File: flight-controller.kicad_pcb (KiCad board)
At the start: 2 copper layers, 51 x 54 mm, 32 parts, among them J1 XT60PW-M, J2 SM04B-SRSS-TB, J3 XT60PW-F, J4 XT60PW-F, J5 XT60PW-F, J6 XT60PW-F, U1 ACS773LCB-100B-PFF, U2 LMR33630ADDA, U3 AMS1117-3.3

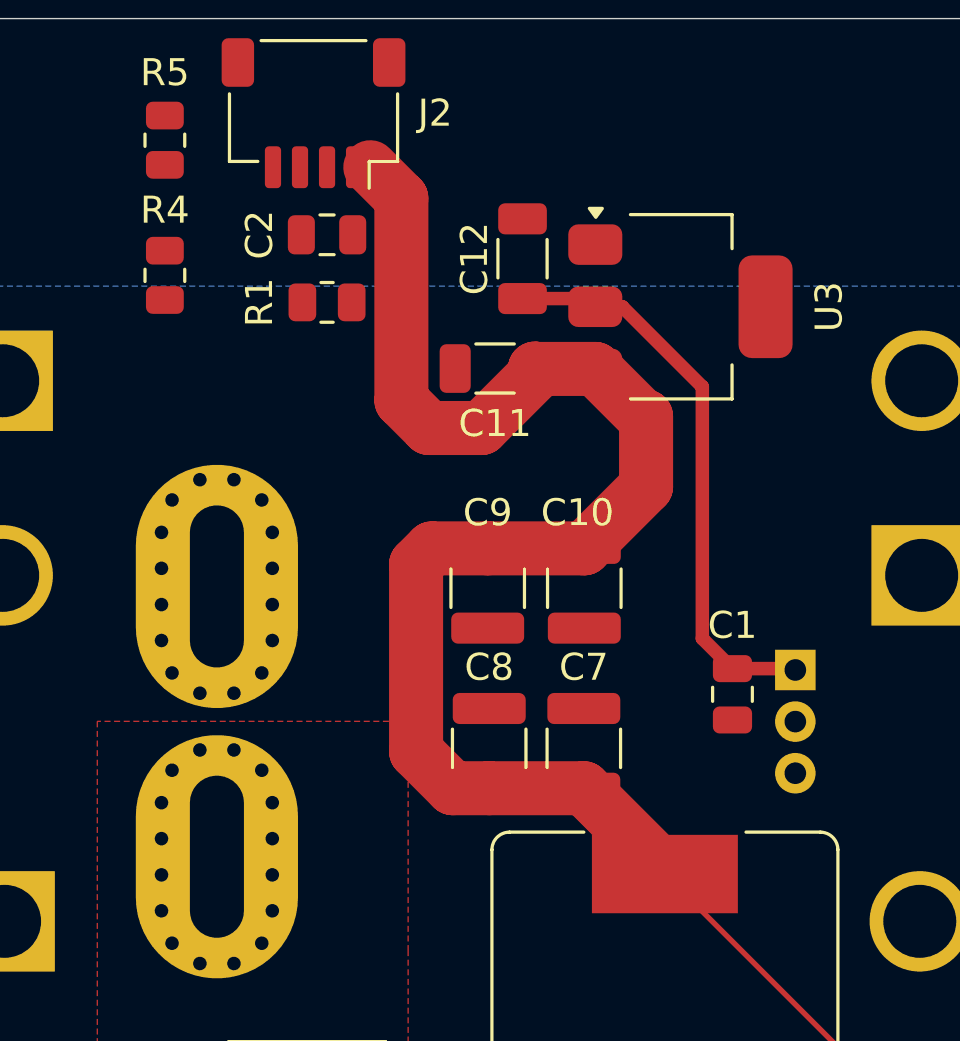
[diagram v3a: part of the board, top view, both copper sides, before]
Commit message: feat: Routed analog signals
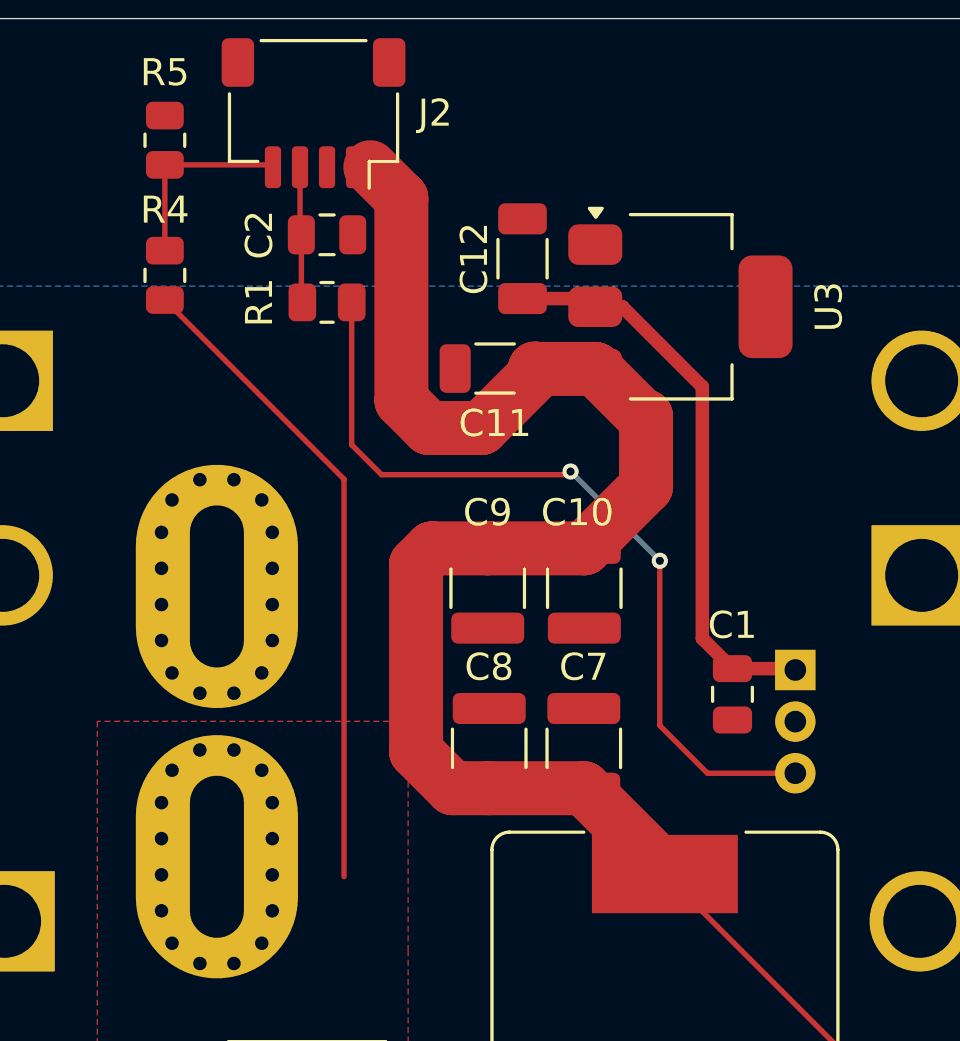
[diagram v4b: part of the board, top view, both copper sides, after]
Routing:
- net Net-(U1-VIOUT): track 0.00 -> 30.4 mm, vias 0 -> 2
- net /VBAT: track 0.00 -> 24.1 mm
- net /VBAT_SENSE: track 0.00 -> 7.21 mm
- net /CURR_SENSE: track 0.00 -> 5.04 mm
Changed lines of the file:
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@@
   (segment (start 145.424 89.662) (end 148.385 92.623) (width 0.5) (layer "F.Cu") (net 1))
   (segment (start 148.385 92.623) (end 148.385 101.935) (width 0.5) (layer "F.Cu") (net 1))
+  (segment (start 133.5 86.95) (end 133.55 87) (width 0.2) (layer "F.Cu") (net 3))
+  (segment (start 133.55 89.4625) (end 133.5875 89.5) (width 0.2) (layer "F.Cu") (net 3))
+  (segment (start 133.5 84.5) (end 133.5 86.95) (width 0.2) (layer "F.Cu") (net 3))
+  (segment (start 133.55 87) (end 133.55 89.4625) (width 0.2) (layer "F.Cu") (net 3))
   (segment (start 152.585 126.015) (end 150.85 126.015) (width 0.5) (layer "F.Cu") (net 4))
   (segment (start 153.15 125.45) (end 152.585 126.015) (width 0.5) (layer "F.Cu") (net 4))
@@
   (segment (start 152.835 127.285) (end 153.05 127.5) (width 0.5) (layer "F.Cu") (net 6))
   (segment (start 150.85 127.285) (end 152.835 127.285) (width 0.5) (layer "F.Cu") (net 6))
+  (segment (start 135.128 96.0405) (end 135.128 110.744) (width 0.2) (layer "F.Cu") (net 7))
+  (segment (start 128.5 89.4125) (end 135.128 96.0405) (width 0.2) (layer "F.Cu") (net 7))
   (segment (start 144.424 91.962) (end 142.205 91.962) (width 2) (layer "F.Cu") (net 8))
   (segment (start 144.018 98.601) (end 146.304 96.315) (width 2) (layer "F.Cu") (net 8))
@@
   (segment (start 153.901166 117.551166) (end 153.901166 122.65) (width 0.2) (layer "F.Cu") (net 8))
   (segment (start 140.214958 94.148) (end 138.267042 94.148) (width 2) (layer "F.Cu") (net 8))
+  (segment (start 128.5 84.4125) (end 132.4125 84.4125) (width 0.2) (layer "F.Cu") (net 9))
+  (segment (start 132.4125 84.4125) (end 132.5 84.5) (width 0.2) (layer "F.Cu") (net 9))
+  (segment (start 128.5 84.4125) (end 128.5 87.5875) (width 0.2) (layer "F.Cu") (net 9))
+  (segment (start 135.4125 94.7725) (end 135.4125 89.5) (width 0.2) (layer "F.Cu") (net 11))
+  (segment (start 136.514815 95.874815) (end 135.4125 94.7725) (width 0.2) (layer "F.Cu") (net 11))
+  (segment (start 146.812 99.06) (end 146.812 105.156) (width 0.2) (layer "F.Cu") (net 11))
+  (segment (start 143.51 95.758) (end 143.393185 95.874815) (width 0.2) (layer "F.Cu") (net 11))
+  (segment (start 146.812 105.156) (end 148.576 106.92) (width 0.2) (layer "F.Cu") (net 11))
+  (segment (start 148.576 106.92) (end 151.825 106.92) (width 0.2) (layer "F.Cu") (net 11))
+  (segment (start 143.393185 95.874815) (end 136.514815 95.874815) (width 0.2) (layer "F.Cu") (net 11))
+  (via (at 146.812 99.06) (size 0.6) (drill 0.3) (layers "F.Cu" "B.Cu") (net 11))
+  (via (at 143.51 95.758) (size 0.6) (drill 0.3) (layers "F.Cu" "B.Cu") (net 11))
+  (segment (start 146.812 99.06) (end 143.51 95.758) (width 0.2) (layer "B.Cu") (net 11))
   (segment (start 150.85 128.9025) (end 150.85 128.555) (width 0.2) (layer "F.Cu") (net 12))
   (segment (start 153.416 131.4685) (end 150.85 128.9025) (width 0.2) (layer "F.Cu") (net 12))

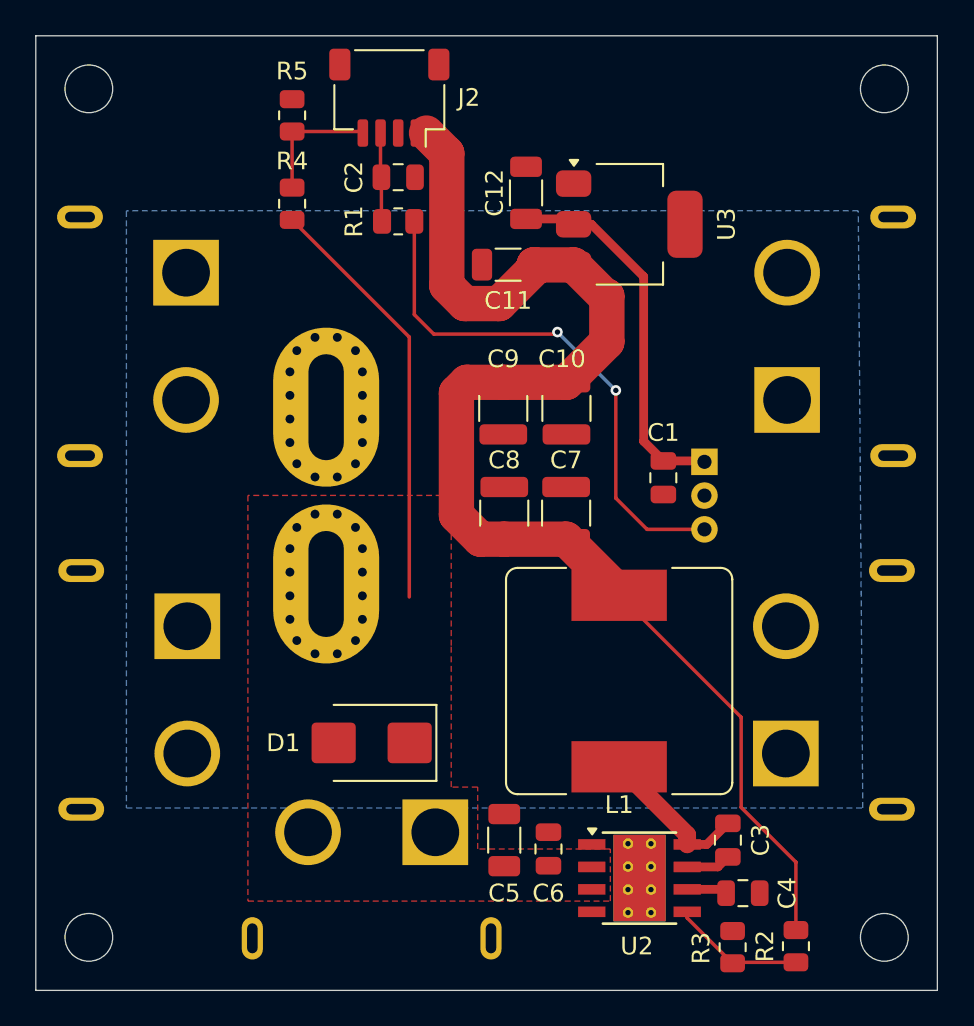
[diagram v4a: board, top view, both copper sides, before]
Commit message: feat: Added both ground planes
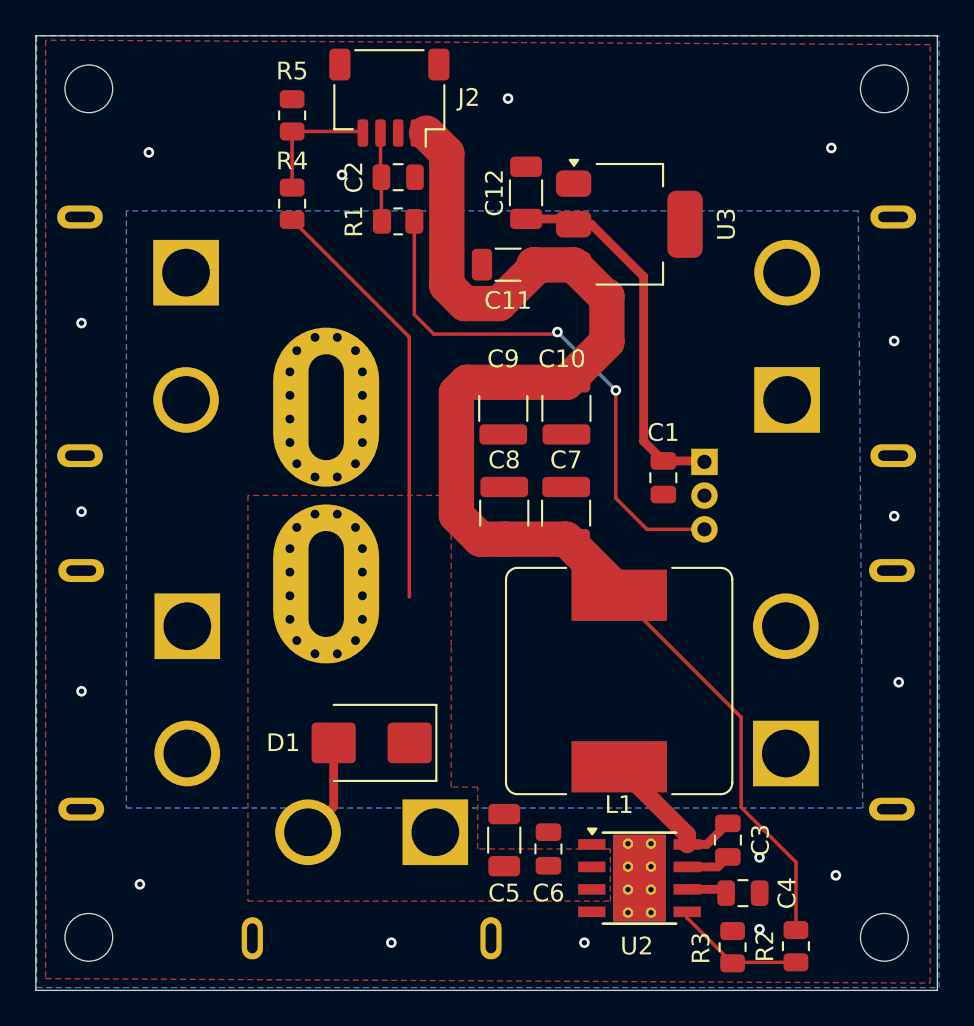
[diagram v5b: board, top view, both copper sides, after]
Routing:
- net GND: track 0.00 -> 5.66 mm, vias 0 -> 16
- added copper zone on B.Cu, net GND
- added copper zone on F.Cu, net GND
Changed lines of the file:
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@@
   (segment (start 145.424 89.662) (end 148.385 92.623) (width 0.5) (layer "F.Cu") (net 1))
   (segment (start 148.385 92.623) (end 148.385 101.935) (width 0.5) (layer "F.Cu") (net 1))
+  (segment (start 130.85 119) (end 130.85 122.605) (width 0.5) (layer "F.Cu") (net 2))
+  (segment (start 130.85 122.605) (end 129.4 124.055) (width 0.5) (layer "F.Cu") (net 2))
+  (via (at 116.586 105.918) (size 0.6) (drill 0.3) (layers "F.Cu" "B.Cu") (free) (net 2))
+  (via (at 140.716 82.55) (size 0.6) (drill 0.3) (layers "F.Cu" "B.Cu") (free) (net 2))
+  (via (at 154.94 129.54) (size 0.6) (drill 0.3) (layers "F.Cu" "B.Cu") (free) (net 2))
+  (via (at 120.396 85.598) (size 0.6) (drill 0.3) (layers "F.Cu" "B.Cu") (free) (net 2))
+  (via (at 162.56 96.266) (size 0.6) (drill 0.3) (layers "F.Cu" "B.Cu") (free) (net 2))
+  (via (at 134.112 130.302) (size 0.6) (drill 0.3) (layers "F.Cu" "B.Cu") (free) (net 2))
+  (via (at 162.56 106.172) (size 0.6) (drill 0.3) (layers "F.Cu" "B.Cu") (free) (net 2))
+  (via (at 145.034 130.302) (size 0.6) (drill 0.3) (layers "F.Cu" "B.Cu") (free) (net 2))
+  (via (at 131.318 86.868) (size 0.6) (drill 0.3) (layers "F.Cu" "B.Cu") (free) (net 2))
+  (via (at 162.814 115.57) (size 0.6) (drill 0.3) (layers "F.Cu" "B.Cu") (free) (net 2))
+  (via (at 159.004 85.344) (size 0.6) (drill 0.3) (layers "F.Cu" "B.Cu") (free) (net 2))
+  (via (at 119.888 127) (size 0.6) (drill 0.3) (layers "F.Cu" "B.Cu") (free) (net 2))
+  (via (at 154.94 125.476) (size 0.6) (drill 0.3) (layers "F.Cu" "B.Cu") (free) (net 2))
+  (via (at 159.258 126.492) (size 0.6) (drill 0.3) (layers "F.Cu" "B.Cu") (free) (net 2))
+  (via (at 116.586 116.078) (size 0.6) (drill 0.3) (layers "F.Cu" "B.Cu") (free) (net 2))
+  (via (at 116.586 95.25) (size 0.6) (drill 0.3) (layers "F.Cu" "B.Cu") (free) (net 2))
   (segment (start 133.5 86.95) (end 133.55 87) (width 0.2) (layer "F.Cu") (net 3))
   (segment (start 133.55 89.4625) (end 133.5875 89.5) (width 0.2) (layer "F.Cu") (net 3))
@@
   (segment (start 157 131.4125) (end 153.472 131.4125) (width 0.2) (layer "F.Cu") (net 12))
   (segment (start 153.472 131.4125) (end 153.416 131.4685) (width 0.2) (layer "F.Cu") (net 12))
+  (zone (net 2) (net_name "GND") (layer "F.Cu") (hatch edge 0.5)
+    (connect_pads yes (clearance 0.2))
+    (min_thickness 0.2) (filled_areas_thickness no)
+    (fill yes (thermal_gap 0.5) (thermal_bridge_width 0.5))
+    (polygon
+      (pts
+        (xy 114.554 79.248)
+        (xy 114.554 132.334)
+        (xy 164.592 132.588)
+        (xy 164.592 79.502)
+      )
+    )
+  )
   (zone (net 7) (net_name "/VBAT") (layer "F.Cu") (hatch edge 0.5)
     (connect_pads yes (clearance 0.5))
@@
     )
   )
+  (zone (net 2) (net_name "GND") (layer "B.Cu") (hatch edge 0.5)
+    (priority 2)
+    (connect_pads yes (clearance 0.2))
+    (min_thickness 0.2) (filled_areas_thickness no)
+    (fill yes (thermal_gap 0.5) (thermal_bridge_width 0.5))
+    (polygon
+      (pts
+        (xy 114.046 78.994)
+        (xy 114.046 132.842)
+        (xy 165.1 132.842)
+        (xy 165.1 78.994)
+      )
+    )
+  )
   (zone (net 10) (net_name "/VBAT_SW") (layer "B.Cu") (hatch edge 0.5)
-    (priority 1)
+    (priority 2)
     (connect_pads yes (clearance 0.5))
     (min_thickness 0.5) (filled_areas_thickness no)

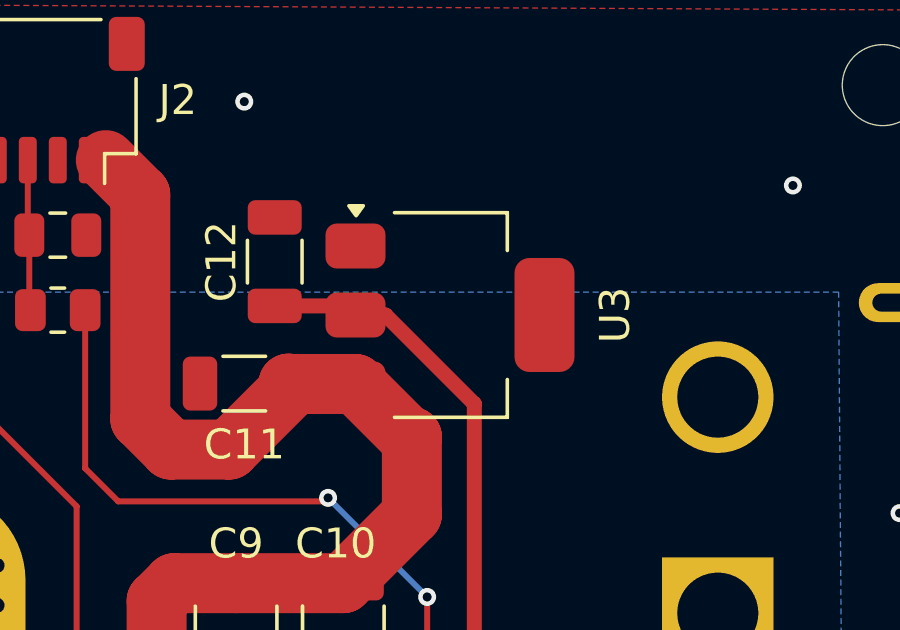
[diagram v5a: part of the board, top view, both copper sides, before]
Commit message: feat: Added 3d models
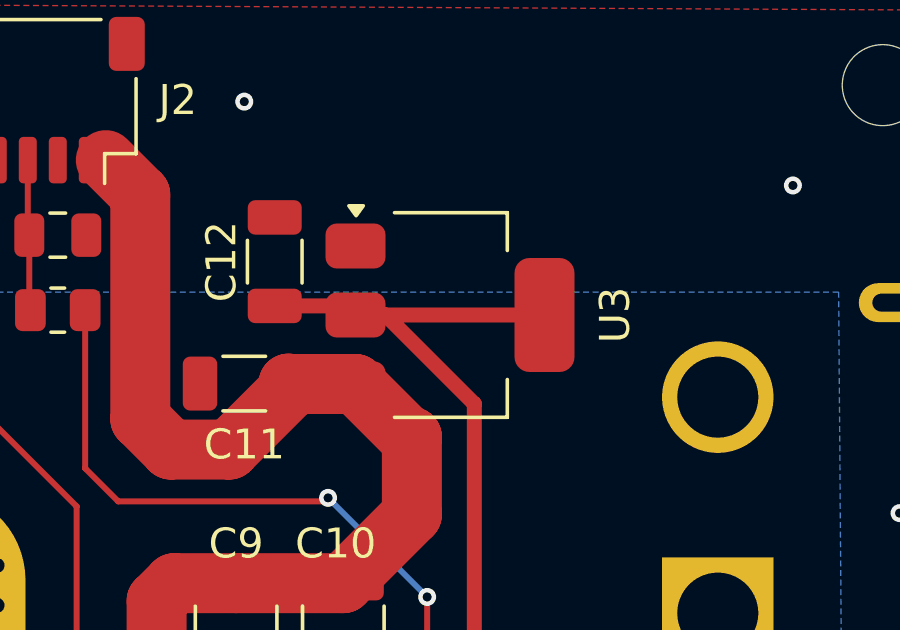
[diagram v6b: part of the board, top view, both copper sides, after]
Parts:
- L1: value 8uH 3.5A -> SRR1260-8R2Y
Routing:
- net +3.3V: track 21.2 -> 27.5 mm
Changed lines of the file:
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@@
         (effects (font (size 1 1) (thickness 0.15)))
     )
-    (fp_text value "8uH 3.5A" (at 0 7.4 90) (layer "F.Fab")
+    (fp_text value "SRR1260-8R2Y" (at 0 7.4 90) (layer "F.Fab")
         (effects (font (size 1 1) (thickness 0.15)))
     )
@@
       (scale (xyz 1 1 1))
       (rotate (xyz 0 0 0))
+    )
+    (model "${KIPRJMOD}/lib/3d_models/SRR1260A.STP"
+      (offset (xyz 0 0 0))
+      (scale (xyz 1 1 1))
+      (rotate (xyz 0 0 -90))
     )
   )
@@
       (rotate (xyz 0 0 0))
     )
+    (model "${KIPRJMOD}/lib/3d_models/LMR33630ADDA.STEP"
+      (offset (xyz 0 0 0))
+      (scale (xyz 1 1 1))
+      (rotate (xyz -90 0 0))
+    )
   )
   (footprint "Connector_JST:JST_SH_SM04B-SRSS-TB_1x04-1MP_P1.00mm_Horizontal" (layer "F.Cu")
@@
         (effects (font (size 1 1) (thickness 0.15)))
     )
-    (fp_text value "SM04B-SRSS-TB" (at 0 3.98) (layer "F.Fab")
+    (fp_text value "SM04B-SRSS-TB" (at -10.018 -0.05) (layer "F.Fab")
         (effects (font (size 1 1) (thickness 0.15)))
     )
@@
       (rotate (xyz 0 0 0))
     )
+    (model "${KIPRJMOD}/lib/3d_models/SM04B-SRSS-TB--3DModel-STEP-269445.STEP"
+      (offset (xyz 0 1.5 0))
+      (scale (xyz 1 1 1))
+      (rotate (xyz 90 -180 -180))
+    )
   )
   (footprint "Capacitor_SMD:C_0805_2012Metric" (layer "F.Cu")
@@
       (rotate (xyz 0 0 0))
     )
+    (model "${KIPRJMOD}/lib/3d_models/AMS1117-3.3.STEP"
+      (offset (xyz 0 0 0))
+      (scale (xyz 1 1 1))
+      (rotate (xyz -90 0 90))
+    )
   )
   (footprint "Capacitor_SMD:C_0805_2012Metric" (layer "F.Cu")
@@
       (scale (xyz 1 1 1))
       (rotate (xyz 0 0 0))
+    )
+    (model "${KIPRJMOD}/lib/3d_models/SMBJ18A.STEP"
+      (offset (xyz 0 0 0))
+      (scale (xyz 1 1 1))
+      (rotate (xyz -90 0 0))
     )
   )
@@
   (segment (start 148.385 101.935) (end 149.5 103.05) (width 0.5) (layer "F.Cu") (net 1))
   (segment (start 151.775 103.05) (end 151.825 103.1) (width 0.5) (layer "F.Cu") (net 1))
+  (segment (start 150.724 89.662) (end 144.424 89.662) (width 0.5) (layer "F.Cu") (net 1))
   (segment (start 149.5 103.05) (end 151.775 103.05) (width 0.5) (layer "F.Cu") (net 1))
   (segment (start 145.424 89.662) (end 148.385 92.623) (width 0.5) (layer "F.Cu") (net 1))
@@
         (xy 137.5 121.5)
         (xy 137.5 113.5)
-        (xy 137.5 113.5)
         (xy 137.5 105)
